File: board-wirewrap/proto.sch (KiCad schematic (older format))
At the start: 46 parts, among them CON101 Micro_SD_Card, P1 AB, P101 Data, P102 Power, P103 DIL8, P2 CD, SW101 RESET, U1 DS8641-LR, U101 Am2908, U102 Am2908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

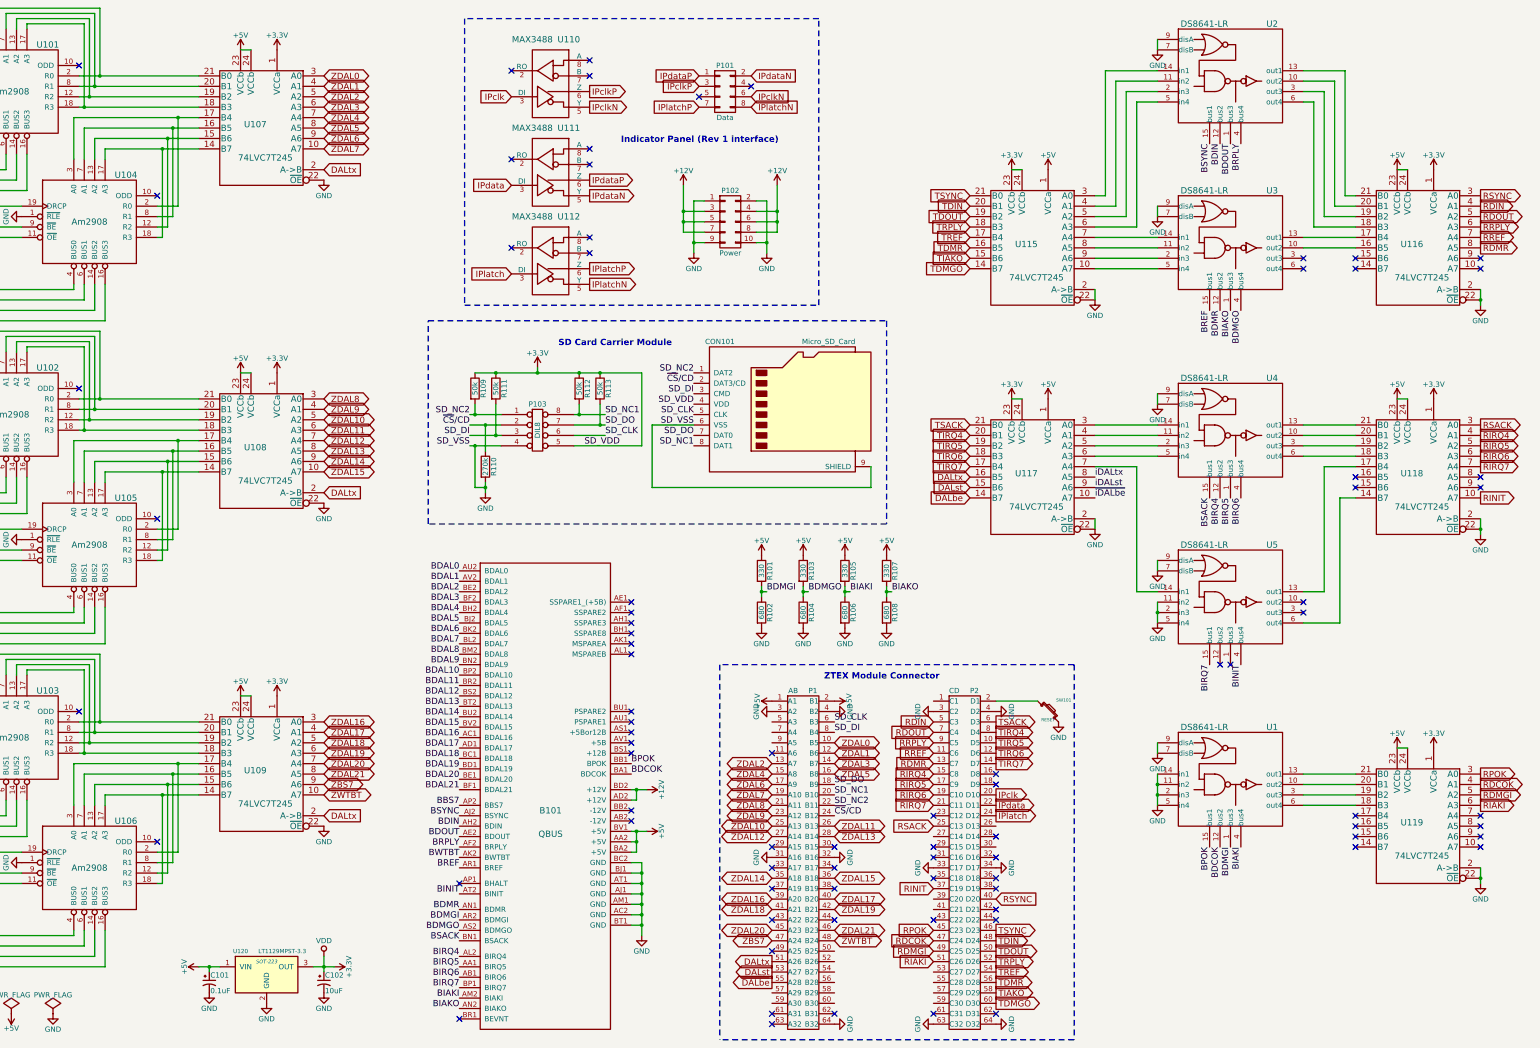
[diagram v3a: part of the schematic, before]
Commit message: Added the LEDs I'm using on the debug board so I keep clear of those FPGA pins
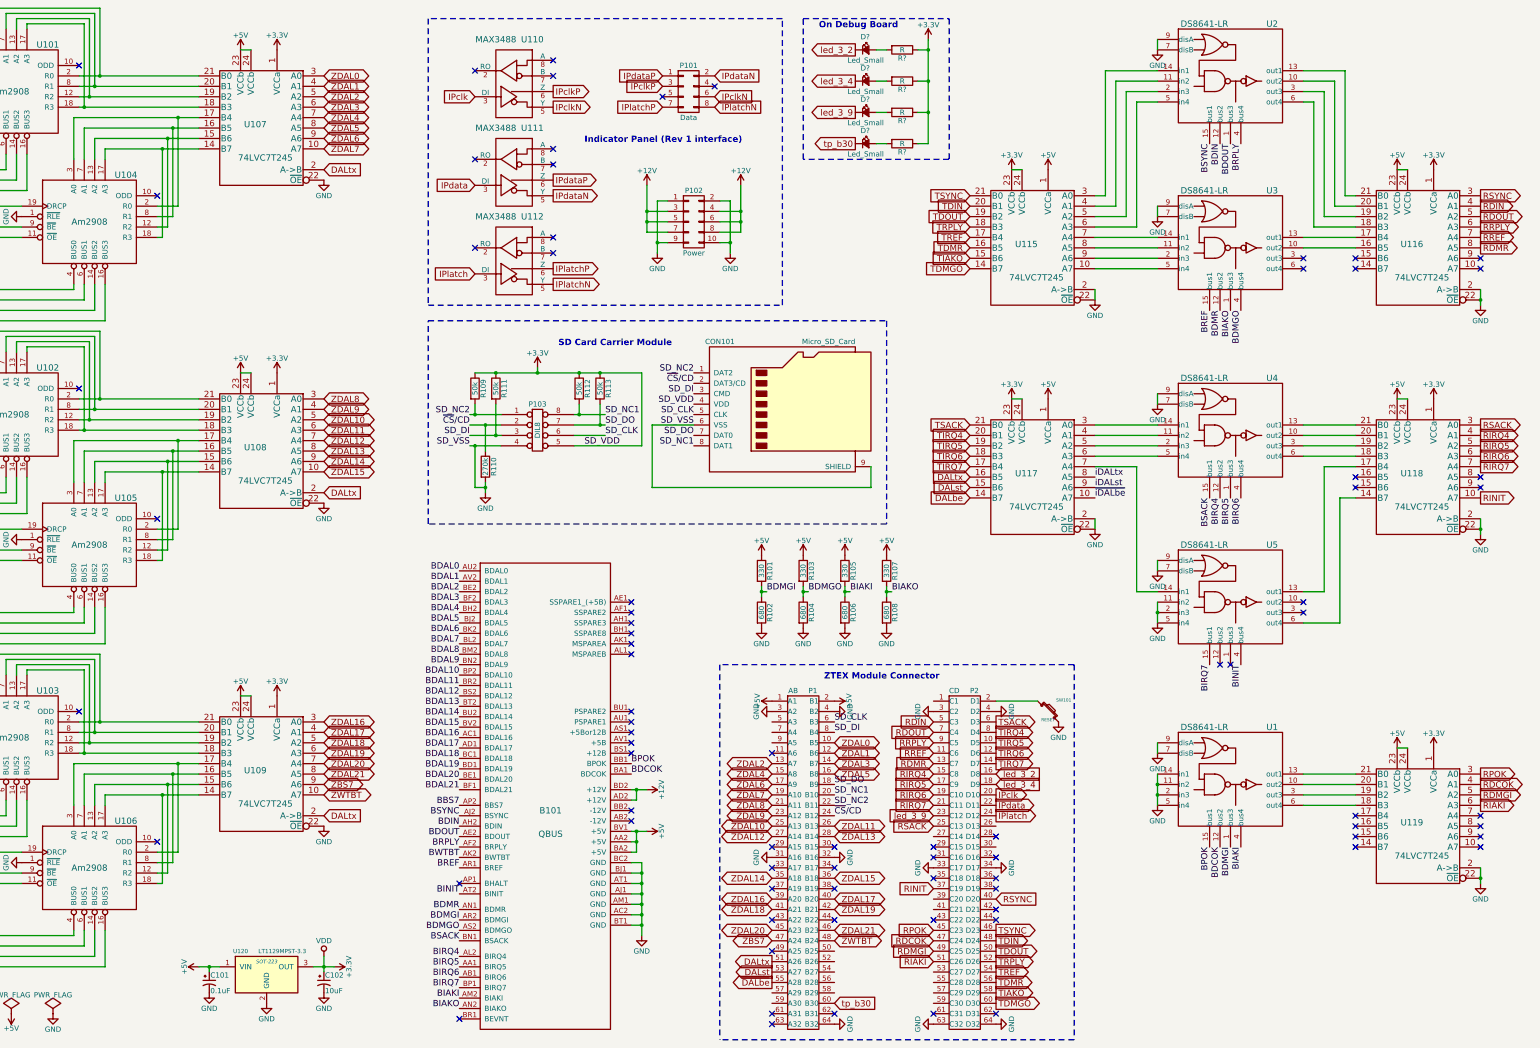
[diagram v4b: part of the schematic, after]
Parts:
- added D? (x4): Led_Small, symbol Led_Small
- added R? (x4): R, symbol R
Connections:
- net +3V3: now also R?.1, R?.1, R?.1, R?.1
- net tp_b30: now reaches P1.60 (B30)
- net tp_b30: now also D?.1 (K)
- net led_3_2: now reaches P2.16 (D8)
- net led_3_2: now also D?.1 (K)
- net led_3_4: now reaches P2.18 (D9)
- net led_3_4: now also D?.1 (K)
- net led_3_9: now reaches P2.23 (C12)
- net led_3_9: now also D?.1 (K)
- new net: D?.2 (A), R?.2 (x4)
- no-connect marks 82 -> 79
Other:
- note added: "On Debug Board"
- moved on the sheet: P101, P102, U110, U111, U112
